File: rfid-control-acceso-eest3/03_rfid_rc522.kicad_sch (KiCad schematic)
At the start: 7 parts, among them J5 RC522_8PIN_3V3_PINOUT_PENDING

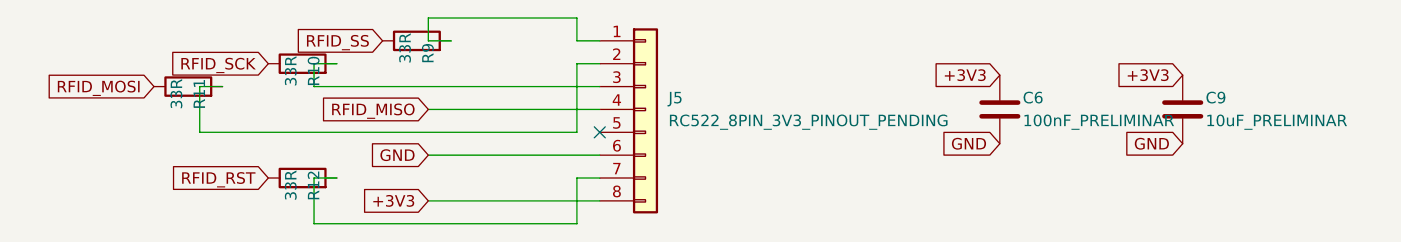
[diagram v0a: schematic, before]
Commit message: Reorganiza floorplan PCB Rev A antes del ruteo
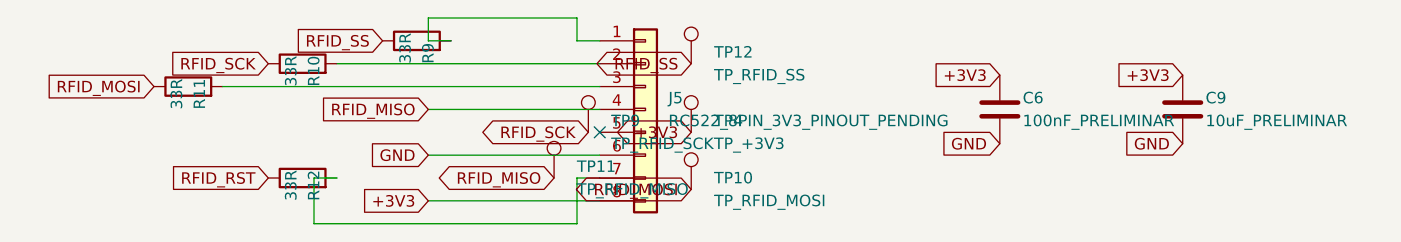
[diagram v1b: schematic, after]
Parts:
- added TP10: TP_RFID_MOSI, TestPoint:TestPoint_THTPad_D2.0mm_Drill1.0mm, symbol Connector:TestPoint
- added TP11: TP_RFID_MISO, TestPoint:TestPoint_THTPad_D2.0mm_Drill1.0mm, symbol Connector:TestPoint
- added TP12: TP_RFID_SS, TestPoint:TestPoint_THTPad_D2.0mm_Drill1.0mm, symbol Connector:TestPoint
- added TP4: TP_+3V3, TestPoint:TestPoint_THTPad_D2.0mm_Drill1.0mm, symbol Connector:TestPoint
- added TP9: TP_RFID_SCK, TestPoint:TestPoint_THTPad_D2.0mm_Drill1.0mm, symbol Connector:TestPoint
- C6: footprint (none) -> Capacitor_THT:C_Disc_D5.0mm_W2.5mm_P5.00mm
- C9: footprint (none) -> rfid_eest3:CP_Radial_D5_P2.00_PLACEHOLDER_NO_FABRICAR
- J5: footprint (none) -> Connector_PinHeader_2.54mm:PinHeader_1x08_P2.54mm_Vertical
- R10, R11, R12, R9: footprint (none) -> Resistor_THT:R_Axial_DIN0207_L6.3mm_D2.5mm_P10.16mm_Horizontal
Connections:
- net +3V3: now also TP4.1
- net RFID_MISO: now also TP11.1
- net RFID_MOSI: now also TP10.1
- net RFID_SCK: now also TP9.1
- net RFID_SS: now also TP12.1
- net at J5.3 (Pin_3), R11.2: no longer J5.2 (Pin_2), R10.2
- new net: J5.2 (Pin_2), R10.2
